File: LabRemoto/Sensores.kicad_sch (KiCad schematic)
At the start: 18 parts

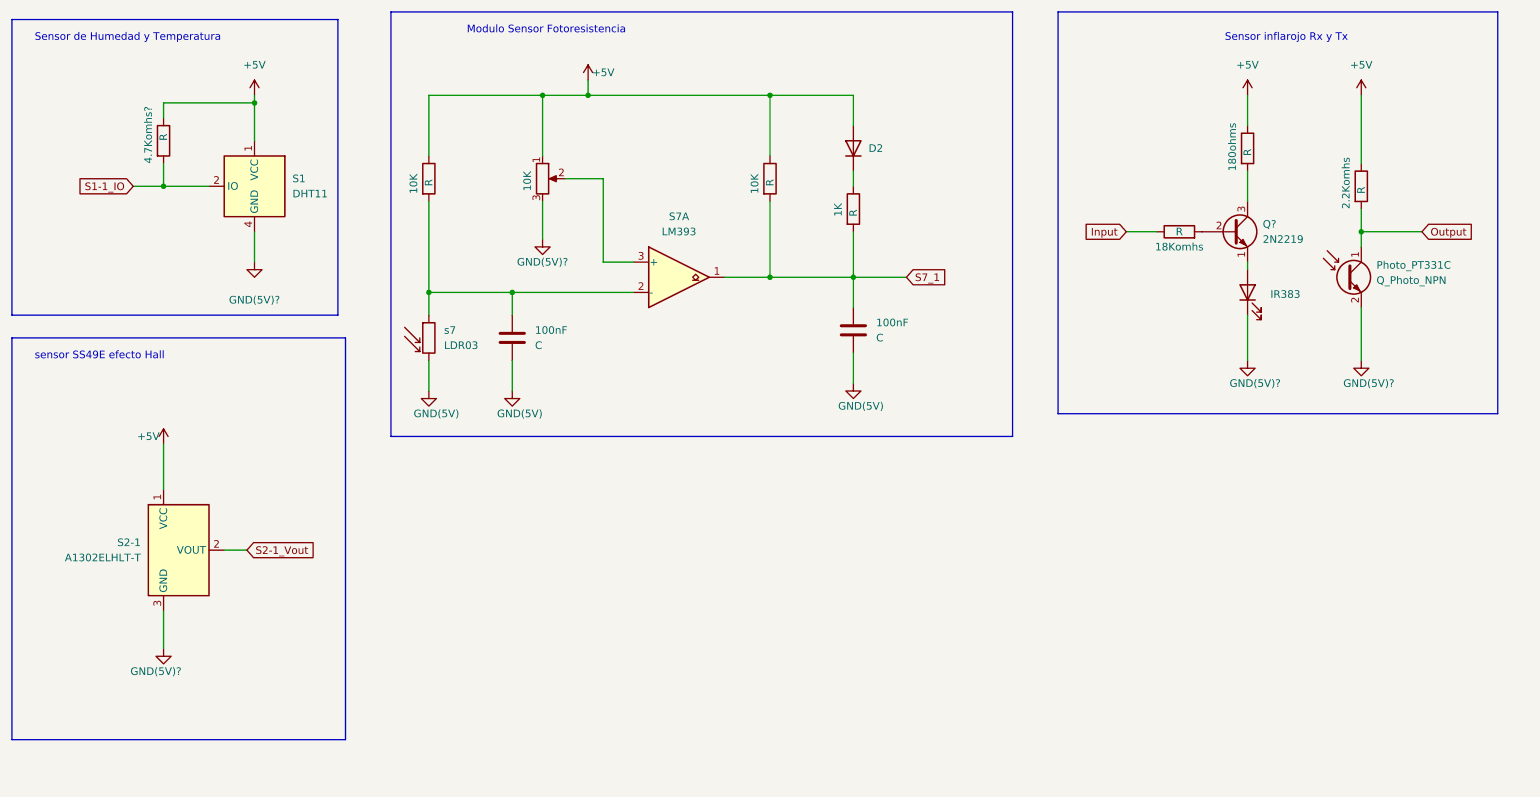
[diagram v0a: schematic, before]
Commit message: Se agrego diagrama rotativo
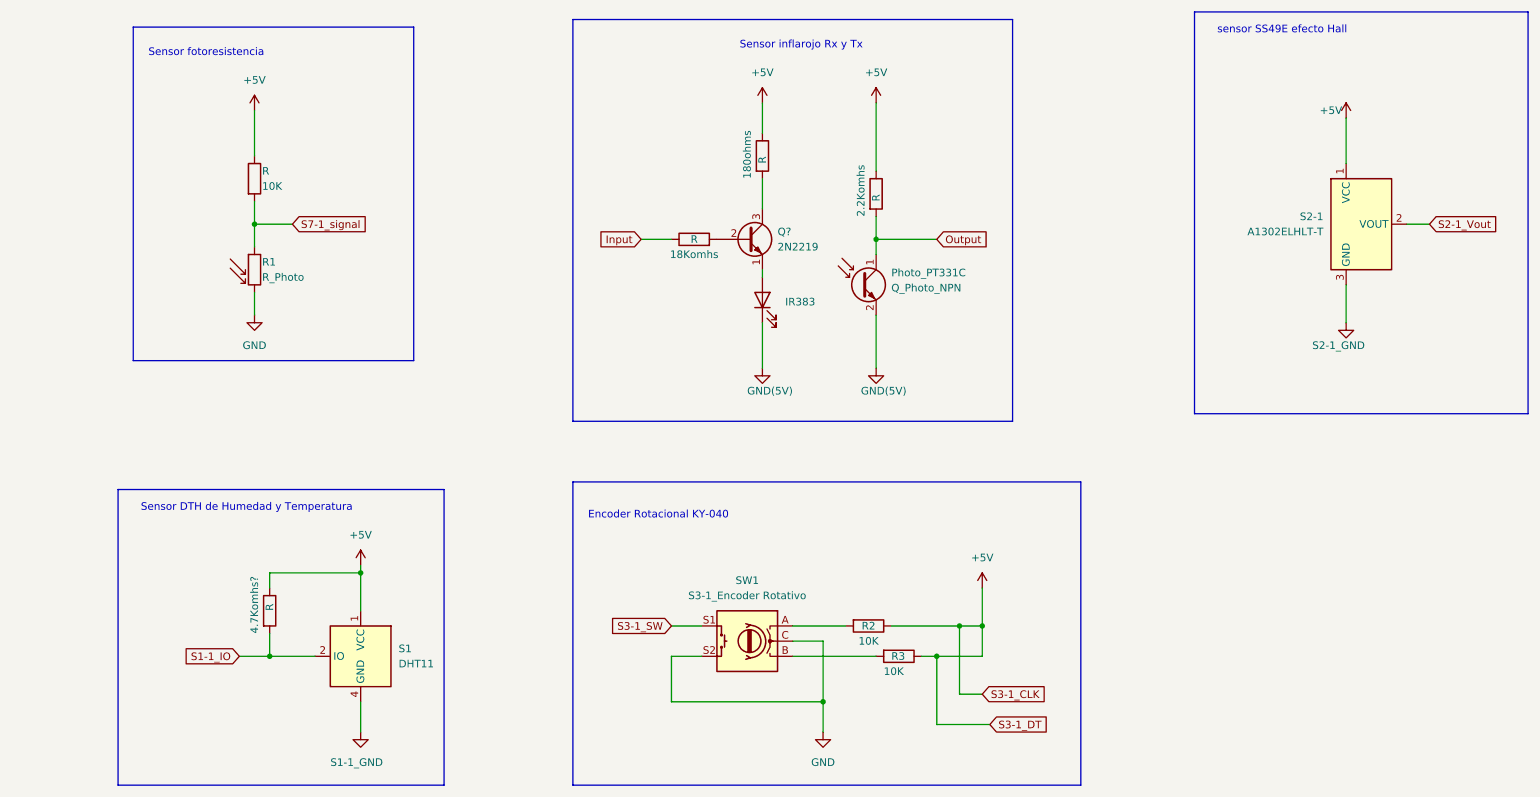
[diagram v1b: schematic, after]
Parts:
- removed 100nF (x2): C, symbol Device:C
- removed 10K: R_Potentiometer, symbol Device:R_Potentiometer
- removed 10K (x2), 1K: R, symbol Device:R
- removed D?: D2, symbol Device:D
- removed S7: LM393, symbol Comparator:LM393
- removed s7: LDR03, OptoDevice:R_LDR_10x8.5mm_P7.6mm_Vertical, symbol Sensor_Optical:LDR03
- added R, R2, R3: 10K, symbol Device:R
- added R1: R_Photo, symbol Device:R_Photo
- added SW1: S3-1_Encoder Rotativo, symbol Device:RotaryEncoder_Switch
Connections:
- net +5V: now also R.1, R2.1, R3.1
- net GND: now also R1.2, SW1.C, SW1.S2
- new net: R2.2, SW1.A
- new net: R3.2, SW1.B
- new net S3-1_SW: SW1.S1
- new net S7-1_signal: R.2, R1.1
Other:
- note added: "Encoder Rotacional KY-040"
- note added: "Sensor DTH de Humedad y Temperatura"
- note added: "Sensor fotoresistencia"
- note removed: "Modulo Sensor Fotoresistencia"
- note removed: "Sensor de Humedad y Temperatura"
- moved on the sheet: 180ohms, 18Komhs, 2.2Komhs, 4.7Komhs?, IR383, Photo_PT331C, Q?, S1, S2-1
